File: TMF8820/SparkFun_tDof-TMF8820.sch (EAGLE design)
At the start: 27 parts, among them J4 QWIIC_RIGHT_ANGLE, J5 QWIIC_RIGHT_ANGLE

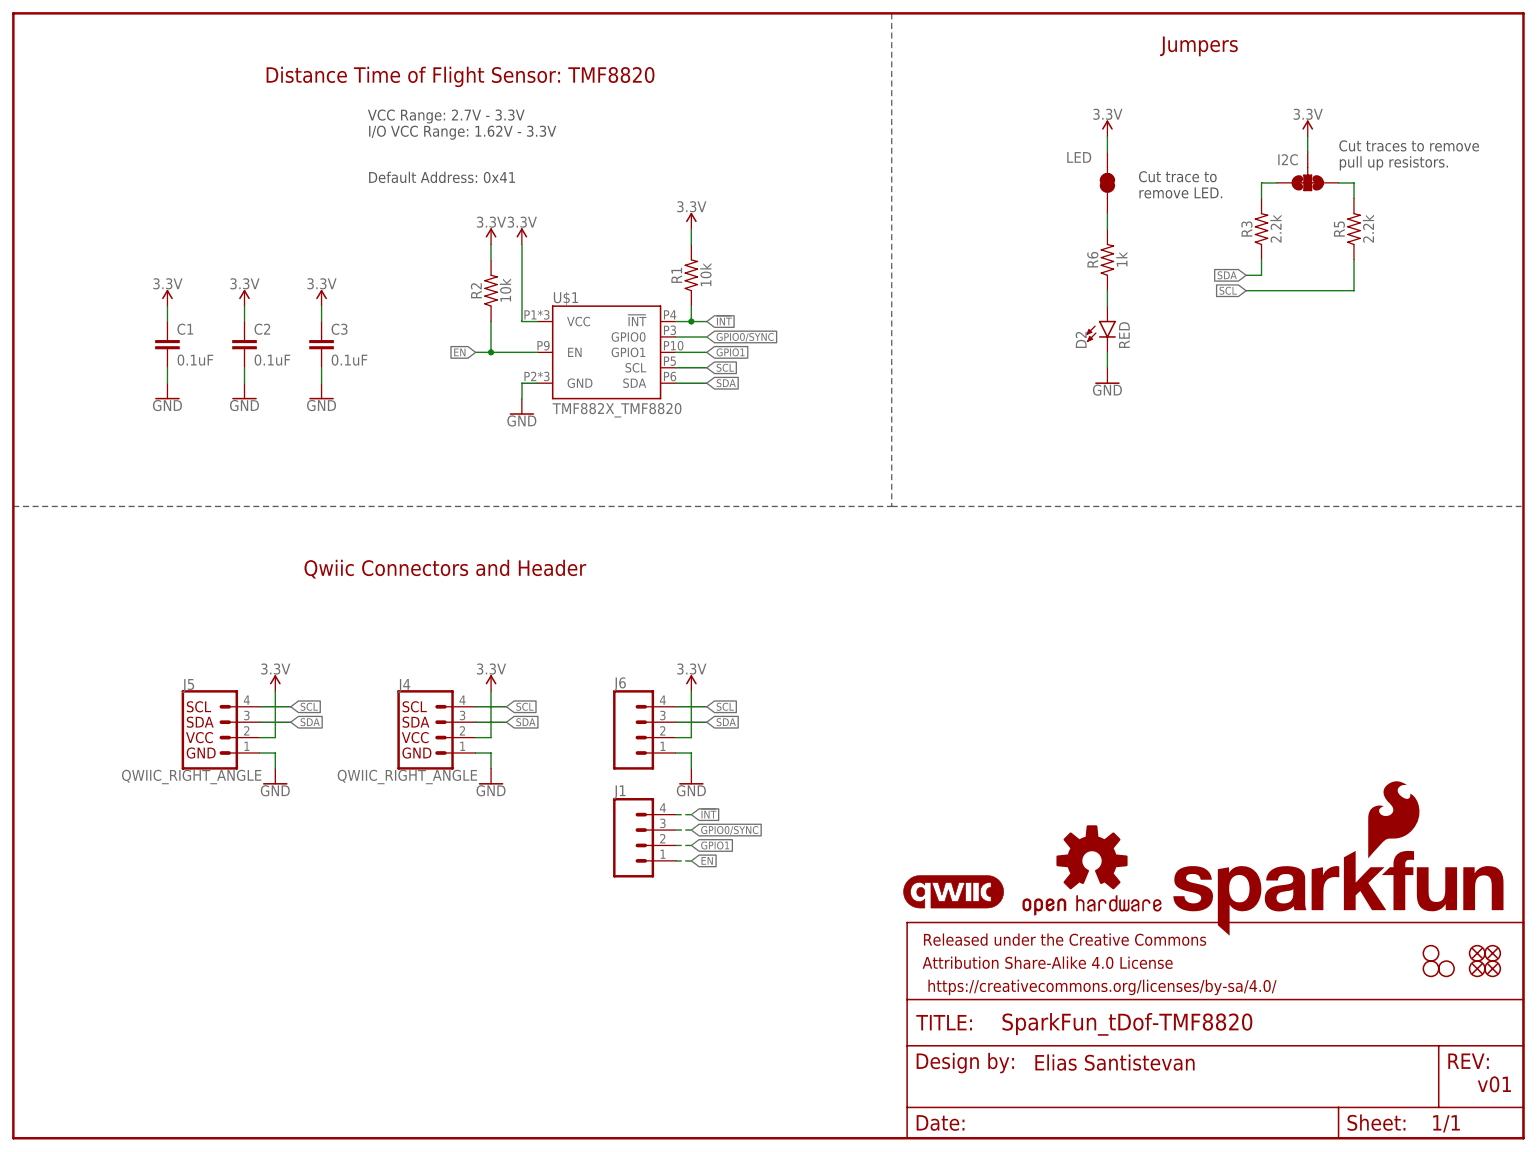
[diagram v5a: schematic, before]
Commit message: Adds a two solder jumper for identifying whether the product has
the 8820 or 8821 - to the 8820 Qwiic Board
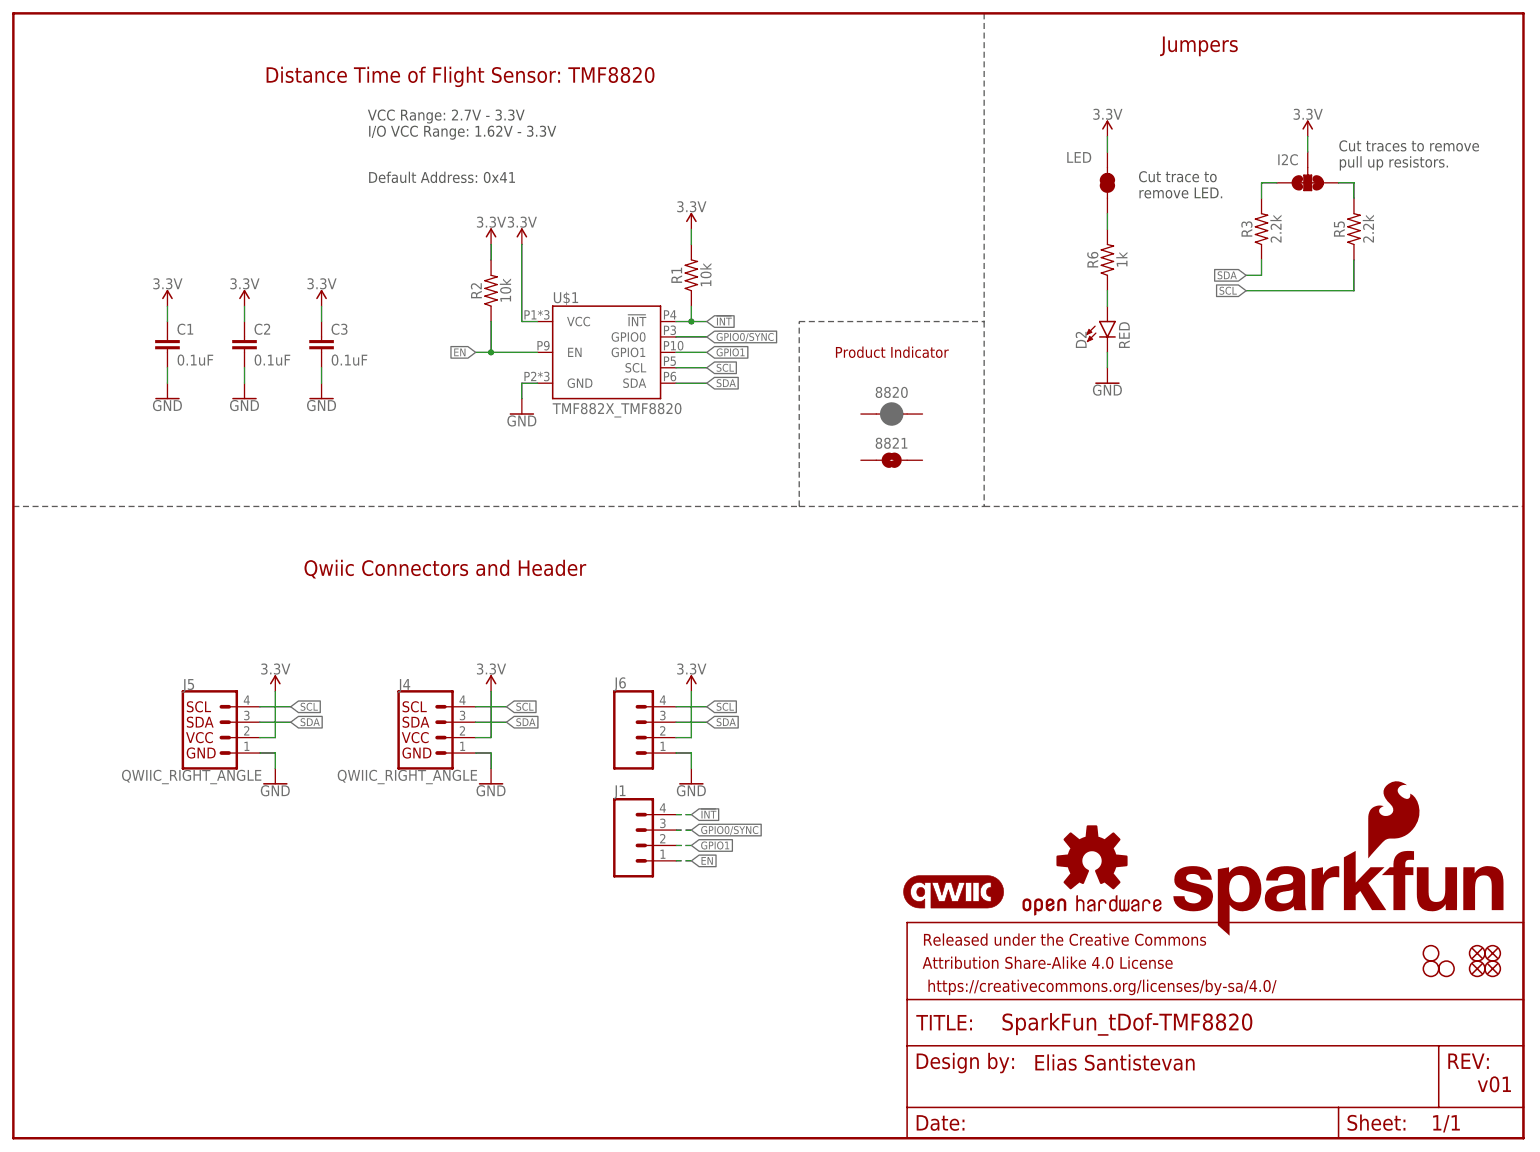
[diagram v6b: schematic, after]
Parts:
- added 8820: JUMPER-SMT_2_NC_PASTE_SILK, SparkFun-Jumpers:JUMPER-SMT_2_NC_PASTE_SILK
- added 8821: JUMPER-SMT_2_NO_SILK, SparkFun-Jumpers:JUMPER-SMT_2_NO_SILK
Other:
- note added: "Product Indicator"
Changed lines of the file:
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@@
 <part name="SUPPLY11" library="SparkFun-PowerSymbols" deviceset="3.3V" device=""/>
 <part name="J1" library="SparkFun-Connectors" deviceset="CONN_04" device="1X04_NO_SILK_NO_POP"/>
+<part name="8820" library="SparkFun-Jumpers" deviceset="JUMPER-SMT_2_NC_PASTE" device="_SILK" package3d_urn="urn:adsk.eagle:package:39282/1"/>
+<part name="8821" library="SparkFun-Jumpers" deviceset="JUMPER-SMT_2_NO" device="_SILK" package3d_urn="urn:adsk.eagle:package:39279/1"/>
 </parts>
 <sheets>
@@
 <text x="168.148" y="11.176" size="2.54" layer="94" font="vector">Elias Santistevan</text>
 <text x="73.66" y="175.26" size="2.54" layer="94" font="vector" align="center">Distance Time of Flight Sensor: TMF8820</text>
-<wire x1="0" y1="104.14" x2="144.78" y2="104.14" width="0.2032" layer="97" style="longdash"/>
-<wire x1="144.78" y1="104.14" x2="248.92" y2="104.14" width="0.2032" layer="97" style="longdash"/>
-<wire x1="144.78" y1="185.42" x2="144.78" y2="104.14" width="0.2032" layer="97" style="longdash"/>
+<wire x1="0" y1="104.14" x2="129.54" y2="104.14" width="0.2032" layer="97" style="longdash"/>
+<wire x1="129.54" y1="104.14" x2="160.02" y2="104.14" width="0.2032" layer="97" style="longdash"/>
+<wire x1="160.02" y1="104.14" x2="248.92" y2="104.14" width="0.2032" layer="97" style="longdash"/>
+<wire x1="160.02" y1="185.42" x2="160.02" y2="134.62" width="0.2032" layer="97" style="longdash"/>
 <text x="58.42" y="165.1" size="1.778" layer="97" font="vector">VCC Range: 2.7V - 3.3V
 I/O VCC Range: 1.62V - 3.3V</text>
 <text x="58.42" y="157.48" size="1.778" layer="97" font="vector">Default Address: 0x41</text>
+<text x="144.78" y="129.54" size="1.778" layer="94" font="vector" align="center">Product Indicator</text>
+<wire x1="160.02" y1="134.62" x2="160.02" y2="104.14" width="0.2032" layer="97" style="longdash"/>
+<wire x1="129.54" y1="104.14" x2="129.54" y2="134.62" width="0.1524" layer="97" style="longdash"/>
+<wire x1="129.54" y1="134.62" x2="160.02" y2="134.62" width="0.1524" layer="97" style="longdash"/>
 </plain>
 <instances>
@@
 <attribute name="NAME" x="99.06" y="56.388" size="1.778" layer="95" font="vector"/>
 </instance>
+<instance part="8820" gate="G$1" x="144.78" y="119.38" smashed="yes">
+<attribute name="NAME" x="144.78" y="122.936" size="1.778" layer="95" font="vector" align="center"/>
+</instance>
+<instance part="8821" gate="G$1" x="144.78" y="111.76" smashed="yes">
+<attribute name="NAME" x="144.78" y="114.554" size="1.778" layer="95" font="vector" align="center"/>
+</instance>
 </instances>

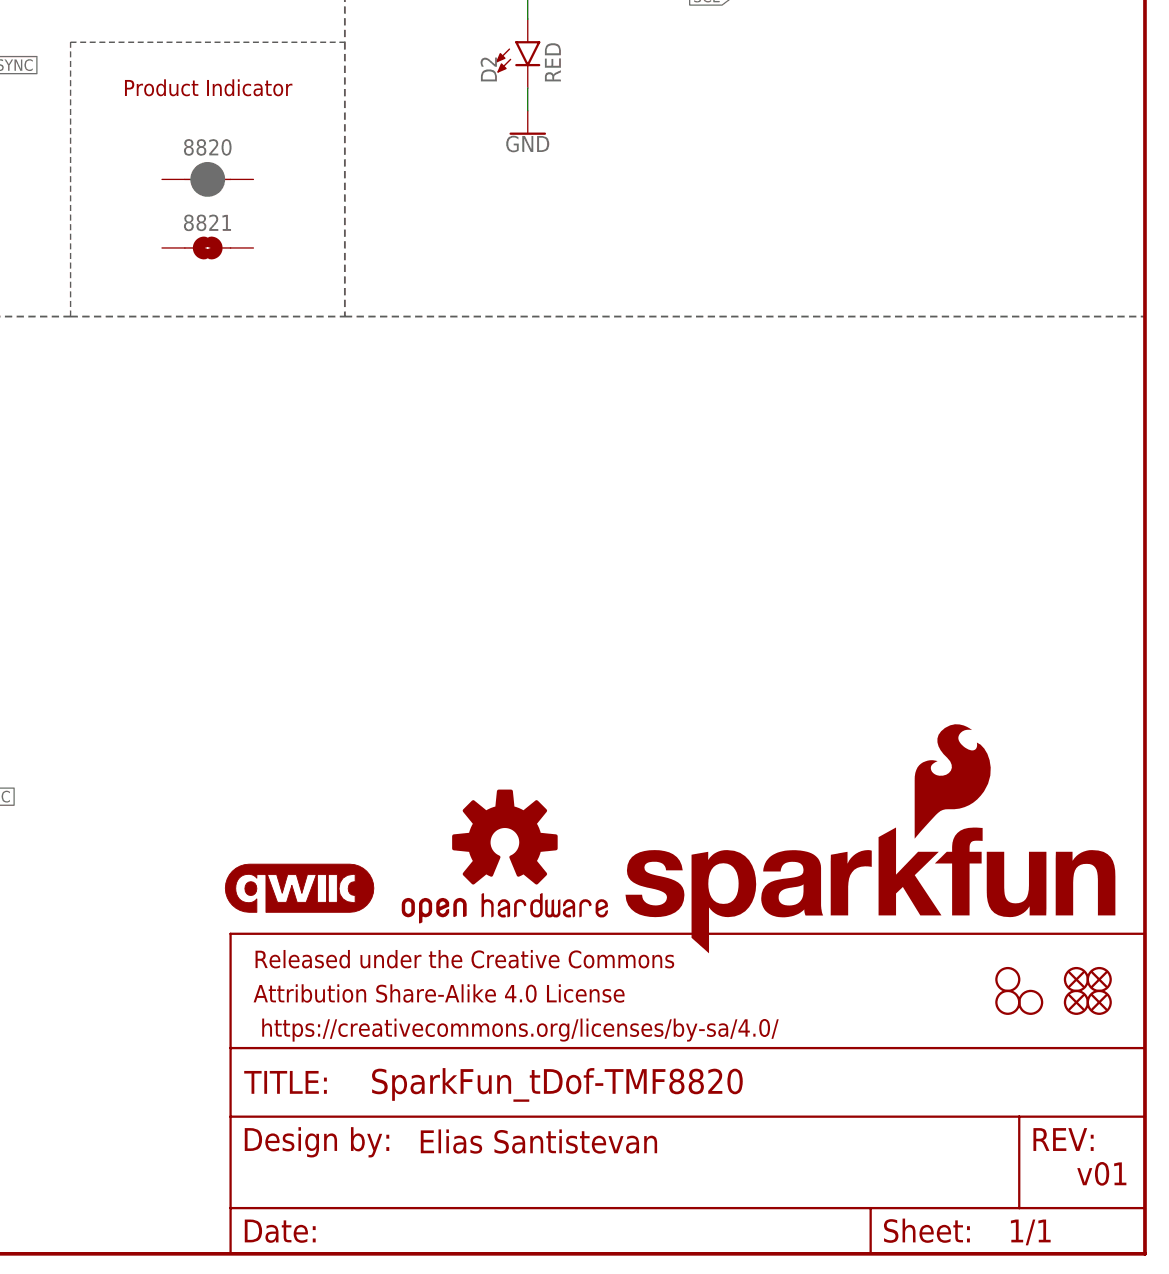
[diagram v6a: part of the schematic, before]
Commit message: Adds new product identifier pads to all designs, rolls 8820 version number to v10
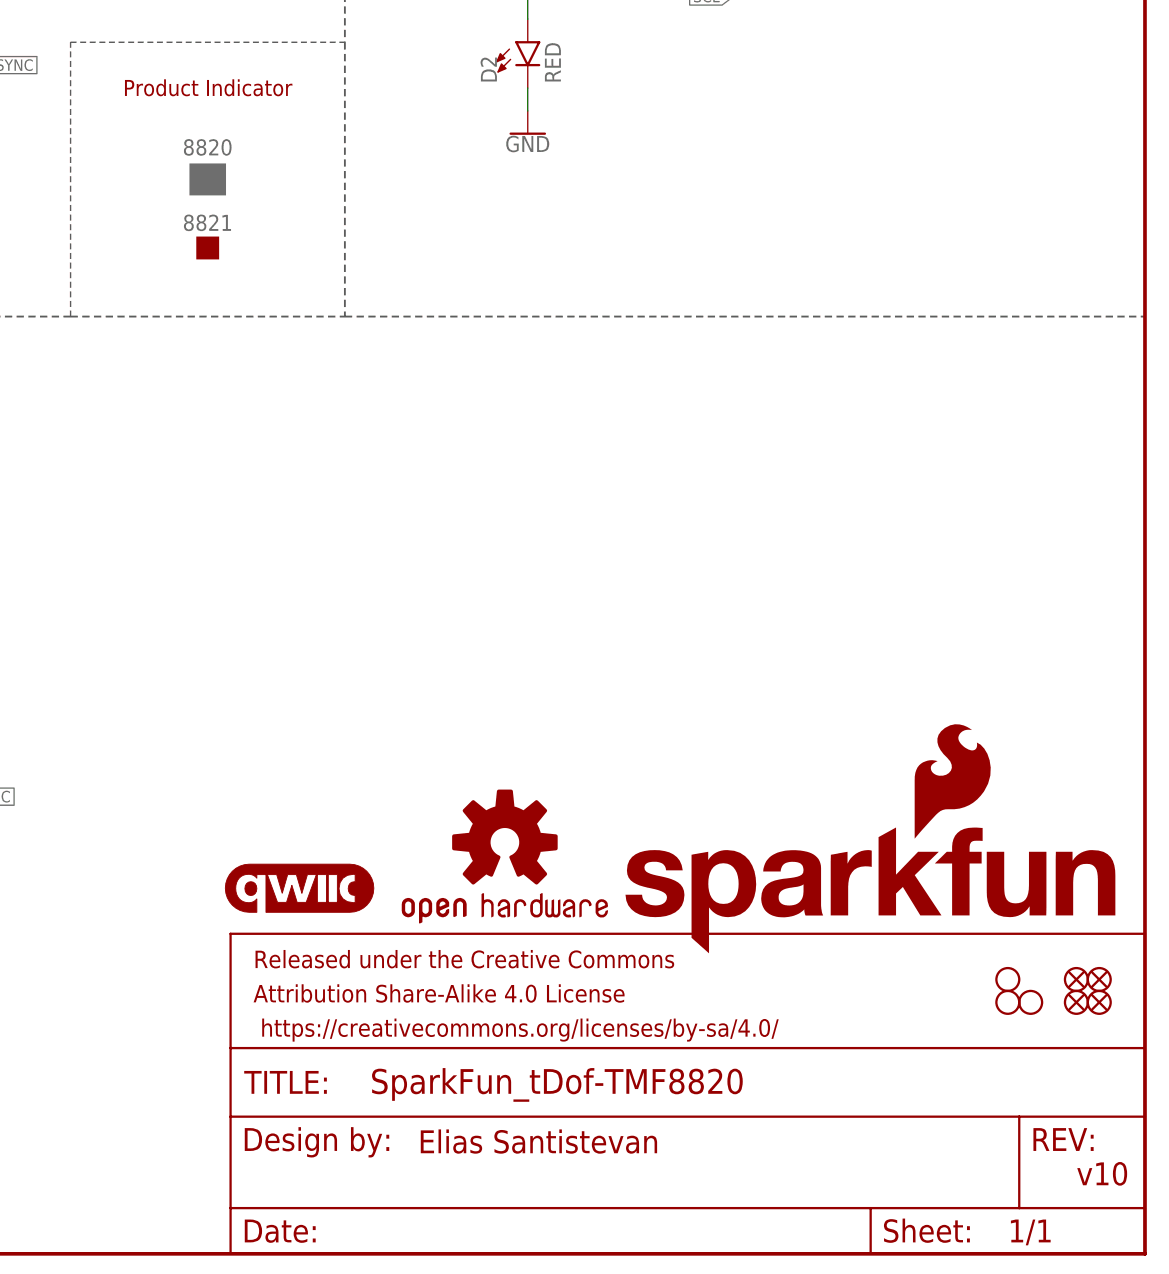
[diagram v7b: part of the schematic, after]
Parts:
- 8820: value JUMPER-SMT_2_NC_PASTE_SILK -> PROD_ID_PASTE_SILK; device SparkFun-Jumpers:JUMPER-SMT_2_NC_PASTE_SILK -> SparkFun-Aesthetics:PROD_ID_PASTE_SILK
- 8821: value JUMPER-SMT_2_NO_SILK -> PROD_ID_NO-PASTE_SILK; device SparkFun-Jumpers:JUMPER-SMT_2_NO_SILK -> SparkFun-Aesthetics:PROD_ID_NO-PASTE_SILK
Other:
- note added: "v10"
- note removed: "v01"
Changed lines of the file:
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@@
 <part name="SUPPLY11" library="SparkFun-PowerSymbols" deviceset="3.3V" device=""/>
 <part name="J1" library="SparkFun-Connectors" deviceset="CONN_04" device="1X04_NO_SILK_NO_POP"/>
-<part name="8820" library="SparkFun-Jumpers" deviceset="JUMPER-SMT_2_NC_PASTE" device="_SILK" package3d_urn="urn:adsk.eagle:package:39282/1"/>
-<part name="8821" library="SparkFun-Jumpers" deviceset="JUMPER-SMT_2_NO" device="_SILK" package3d_urn="urn:adsk.eagle:package:39279/1"/>
+<part name="8820" library="SparkFun-Aesthetics" deviceset="PROD_ID_PASTE" device="_SILK"/>
+<part name="8821" library="SparkFun-Aesthetics" deviceset="PROD_ID_NO-PASTE" device="_SILK"/>
 </parts>
 <sheets>
 <sheet>
 <plain>
-<text x="241.3" y="7.62" size="2.54" layer="94" font="vector">v01</text>
+<text x="241.3" y="7.62" size="2.54" layer="94" font="vector">v10</text>
 <text x="71.12" y="93.98" size="2.54" layer="94" font="vector" align="center">Qwiic Connectors and Header</text>
 <text x="195.58" y="180.34" size="2.54" layer="94" font="vector" align="center">Jumpers</text>
